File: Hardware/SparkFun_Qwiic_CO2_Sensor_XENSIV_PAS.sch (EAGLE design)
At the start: 39 parts, among them J1 QWIIC_RA, J2 QWIIC_RA, U1 PASCO2V01BUMA1, U2 LMR62421

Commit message: Update pre design review
Add keepouts for exposed pads.
Move vias to avoid keepouts.
Add 10k PUR to PSEL 3.3V selector.
Add voltage/current details to CO2 sensor on schematic.
Modified bottom PTHs to match standard order.
Move vias for ground pour.
Remove ground stub and unnecessary tRestrict.
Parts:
- added R7: 10k, SparkFun-Resistors:10KOHM-0603-1/10W-1%
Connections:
- new net N$8: PSEL.1, R7.1
- net 3.3V: now also J4.3, R7.2; no longer J4.2, PSEL.1
- net GND: now also J4.2; no longer J4.5
- net SCL: now also J4.5; no longer J4.4
- net SDA/TX: now also J4.4; no longer J4.3
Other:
- note added: "Power requirements: 3.3V - 10mA peak, 6.1mA average 12V - 130mA peak, 0.8mA average"
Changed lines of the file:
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@@
 <part name="GND14" library="SparkFun-PowerSymbols" deviceset="GND" device=""/>
 <part name="GND15" library="SparkFun-PowerSymbols" deviceset="GND" device=""/>
-<part name="GND16" library="SparkFun-PowerSymbols" deviceset="GND" device=""/>
-<part name="SUPPLY10" library="SparkFun-PowerSymbols" deviceset="3.3V" device=""/>
 <part name="SUPPLY11" library="SparkFun-PowerSymbols" deviceset="3.3V" device=""/>
 <part name="SUPPLY12" library="SparkFun-PowerSymbols" deviceset="3.3V" device=""/>
@@
 <part name="GND17" library="SparkFun-PowerSymbols" deviceset="GND" device=""/>
 <part name="PWR" library="SparkFun-Jumpers" deviceset="JUMPER-SMT_2_NC_TRACE" device="_SILK" package3d_urn="urn:adsk.eagle:package:39281/1"/>
+<part name="R7" library="SparkFun-Resistors" deviceset="10KOHM" device="-0603-1/10W-1%" value="10k"/>
+<part name="GND16" library="SparkFun-PowerSymbols" deviceset="GND" device=""/>
+<part name="SUPPLY10" library="SparkFun-PowerSymbols" deviceset="3.3V" device=""/>
 </parts>
 <sheets>
@@
 Output: 12V @ 350mA</text>
 <text x="48.26" y="96.52" size="1.778" layer="97" font="vector">7-bit unshifted address: 0x28</text>
+<text x="53.34" y="81.28" size="1.778" layer="97" font="vector">Power requirements:
+3.3V - 10mA peak, 6.1mA average
+12V - 130mA peak, 0.8mA average</text>
 </plain>
 <instances>
@@
 <attribute name="NAME" x="38.1" y="116.84" size="1.778" layer="95" font="vector" rot="MR180" align="center-right"/>
 </instance>
-<instance part="SUPPLY8" gate="G$1" x="40.64" y="124.46" smashed="yes">
-<attribute name="VALUE" x="40.64" y="127.254" size="1.778" layer="96" font="vector" align="bottom-center"/>
+<instance part="SUPPLY8" gate="G$1" x="40.64" y="137.16" smashed="yes">
+<attribute name="VALUE" x="40.64" y="139.954" size="1.778" layer="96" font="vector" align="bottom-center"/>
 </instance>
 <instance part="GND11" gate="1" x="40.64" y="106.68" smashed="yes">
@@
 <attribute name="VALUE" x="226.06" y="78.486" size="1.778" layer="96" font="vector" align="top-center"/>
 </instance>
-<instance part="GND16" gate="1" x="200.66" y="91.44" smashed="yes">
-<attribute name="VALUE" x="200.66" y="91.186" size="1.778" layer="96" font="vector" align="top-center"/>
-</instance>
-<instance part="SUPPLY10" gate="G$1" x="200.66" y="109.22" smashed="yes">
-<attribute name="VALUE" x="200.66" y="112.014" size="1.778" layer="96" font="vector" align="bottom-center"/>
-</instance>
 <instance part="SUPPLY11" gate="G$1" x="226.06" y="121.92" smashed="yes">
 <attribute name="VALUE" x="226.06" y="124.714" size="1.778" layer="96" font="vector" align="bottom-center"/>
@@
 <instance part="PWR" gate="G$1" x="154.94" y="137.16" smashed="yes" rot="R90">
 <attribute name="NAME" x="160.02" y="136.652" size="1.778" layer="95" font="vector" rot="R180" align="center"/>
+</instance>
+<instance part="R7" gate="G$1" x="40.64" y="129.54" smashed="yes" rot="R90">
+<attribute name="NAME" x="39.116" y="129.54" size="1.778" layer="95" font="vector" rot="R90" align="bottom-center"/>
+<attribute name="VALUE" x="42.164" y="129.54" size="1.778" layer="96" font="vector" rot="R90" align="top-center"/>
+</instance>
+<instance part="GND16" gate="1" x="203.2" y="88.9" smashed="yes">
+<attribute name="VALUE" x="203.2" y="88.646" size="1.778" layer="96" font="vector" align="top-center"/>
+</instance>
+<instance part="SUPPLY10" gate="G$1" x="200.66" y="109.22" smashed="yes">
+<attribute name="VALUE" x="200.66" y="112.014" size="1.778" layer="96" font="vector" align="bottom-center"/>
 </instance>
 </instances>
@@
 </segment>
 <segment>
-<wire x1="200.66" y1="96.52" x2="200.66" y2="93.98" width="0.1524" layer="91"/>
-<pinref part="GND16" gate="1" pin="GND"/>
-<pinref part="J4" gate="J1" pin="5"/>
-<wire x1="198.12" y1="96.52" x2="200.66" y2="96.52" width="0.1524" layer="91"/>
-</segment>
-<segment>
 <wire x1="226.06" y1="142.24" x2="226.06" y2="137.16" width="0.1524" layer="91"/>
 <pinref part="GND12" gate="1" pin="GND"/>
@@
 <wire x1="154.94" y1="109.22" x2="154.94" y2="106.68" width="0.1524" layer="91"/>
 <pinref part="GND17" gate="1" pin="GND"/>
+</segment>
+<segment>
+<wire x1="203.2" y1="104.14" x2="203.2" y2="91.44" width="0.1524" layer="91"/>
+<pinref part="GND16" gate="1" pin="GND"/>
+<wire x1="198.12" y1="104.14" x2="203.2" y2="104.14" width="0.1524" layer="91"/>
+<pinref part="J4" gate="J1" pin="2"/>
 </segment>
 </net>
@@
 </segment>
 <segment>
-<pinref part="SUPPLY8" gate="G$1" pin="3.3V"/>
-<wire x1="40.64" y1="124.46" x2="40.64" y2="121.92" width="0.1524" layer="91"/>
-<pinref part="PSEL" gate="G$1" pin="1"/>
-</segment>
-<segment>
-<pinref part="SUPPLY10" gate="G$1" pin="3.3V"/>
-<wire x1="200.66" y1="109.22" x2="200.66" y2="104.14" width="0.1524" layer="91"/>
-<pinref part="J4" gate="J1" pin="2"/>
-<wire x1="198.12" y1="104.14" x2="200.66" y2="104.14" width="0.1524" layer="91"/>
-</segment>
-<segment>
 <pinref part="SUPPLY11" gate="G$1" pin="3.3V"/>
 <wire x1="226.06" y1="121.92" x2="226.06" y2="114.3" width="0.1524" layer="91"/>
@@
 <pinref part="SUPPLY13" gate="G$1" pin="3.3V"/>
 <wire x1="154.94" y1="142.24" x2="154.94" y2="144.78" width="0.1524" layer="91"/>
+</segment>
+<segment>
+<pinref part="SUPPLY8" gate="G$1" pin="3.3V"/>
+<pinref part="R7" gate="G$1" pin="2"/>
+<wire x1="40.64" y1="137.16" x2="40.64" y2="134.62" width="0.1524" layer="91"/>
+</segment>
+<segment>
+<pinref part="SUPPLY10" gate="G$1" pin="3.3V"/>
+<wire x1="200.66" y1="109.22" x2="200.66" y2="101.6" width="0.1524" layer="91"/>
+<wire x1="198.12" y1="101.6" x2="200.66" y2="101.6" width="0.1524" layer="91"/>
+<pinref part="J4" gate="J1" pin="3"/>
 </segment>
 </net>
@@
 <segment>
 <wire x1="198.12" y1="106.68" x2="203.2" y2="106.68" width="0.1524" layer="91"/>
+<label x="203.2" y="106.68" size="1.27" layer="95" font="vector" xref="yes"/>
 <pinref part="J4" gate="J1" pin="1"/>
-<label x="203.2" y="106.68" size="1.27" layer="95" font="vector" xref="yes"/>
 </segment>
 </net>
@@
 </segment>
 <segment>
-<wire x1="218.44" y1="91.44" x2="218.44" y2="99.06" width="0.1524" layer="91"/>
 <pinref part="J1" gate="J1" pin="4"/>
-<wire x1="218.44" y1="99.06" x2="218.44" y2="119.38" width="0.1524" layer="91"/>
+<wire x1="218.44" y1="91.44" x2="218.44" y2="96.52" width="0.1524" layer="91"/>
+<wire x1="218.44" y1="96.52" x2="218.44" y2="119.38" width="0.1524" layer="91"/>
 <wire x1="218.44" y1="119.38" x2="228.6" y2="119.38" width="0.1524" layer="91"/>
 <pinref part="J2" gate="J1" pin="4"/>
@@
 <junction x="218.44" y="119.38"/>
 <label x="215.9" y="119.38" size="1.27" layer="95" font="vector" rot="R180" xref="yes"/>
-<pinref part="J4" gate="J1" pin="4"/>
-<wire x1="198.12" y1="99.06" x2="218.44" y2="99.06" width="0.1524" layer="91"/>
-<junction x="218.44" y="99.06"/>
+<wire x1="198.12" y1="96.52" x2="218.44" y2="96.52" width="0.1524" layer="91"/>
+<pinref part="J4" gate="J1" pin="5"/>
+<junction x="218.44" y="96.52"/>
 </segment>
 </net>
@@
 <wire x1="228.6" y1="116.84" x2="220.98" y2="116.84" width="0.1524" layer="91"/>
 <pinref part="J2" gate="J1" pin="3"/>
-<wire x1="220.98" y1="116.84" x2="220.98" y2="101.6" width="0.1524" layer="91"/>
-<wire x1="220.98" y1="101.6" x2="220.98" y2="88.9" width="0.1524" layer="91"/>
+<wire x1="220.98" y1="116.84" x2="220.98" y2="99.06" width="0.1524" layer="91"/>
+<wire x1="220.98" y1="99.06" x2="220.98" y2="88.9" width="0.1524" layer="91"/>
 <wire x1="220.98" y1="88.9" x2="228.6" y2="88.9" width="0.1524" layer="91"/>
-<pinref part="J4" gate="J1" pin="3"/>
-<wire x1="198.12" y1="101.6" x2="220.98" y2="101.6" width="0.1524" layer="91"/>
-<junction x="220.98" y="101.6"/>
 <wire x1="220.98" y1="116.84" x2="215.9" y2="116.84" width="0.1524" layer="91"/>
 <junction x="220.98" y="116.84"/>
 <label x="215.9" y="116.84" size="1.27" layer="95" font="vector" rot="R180" xref="yes"/>
+<wire x1="198.12" y1="99.06" x2="220.98" y2="99.06" width="0.1524" layer="91"/>
+<pinref part="J4" gate="J1" pin="4"/>
+<junction x="220.98" y="99.06"/>
 </segment>
 <segment>
@@
 </segment>
 </net>
+<net name="N$8" class="0">
+<segment>
+<pinref part="R7" gate="G$1" pin="1"/>
+<pinref part="PSEL" gate="G$1" pin="1"/>
+<wire x1="40.64" y1="124.46" x2="40.64" y2="121.92" width="0.1524" layer="91"/>
+</segment>
+</net>

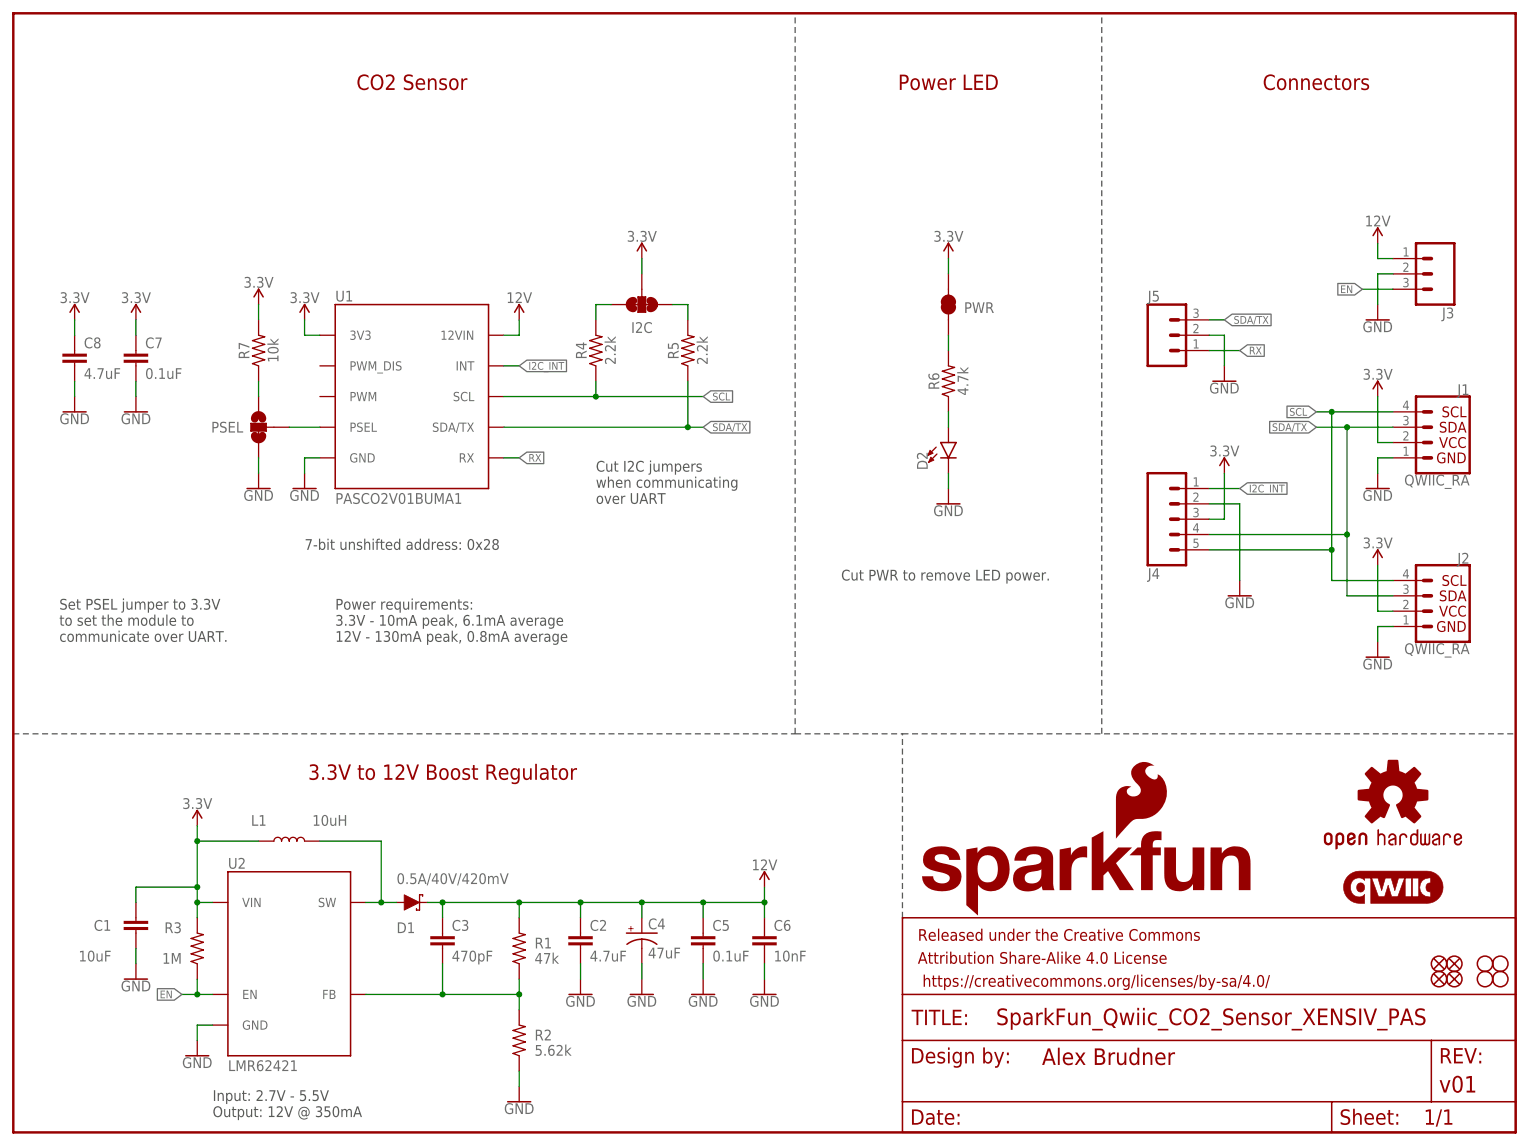
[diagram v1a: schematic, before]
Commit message: Post design review changes and gerbers.
Add tDocu for the can and put squares for PnP.
Move EN to bottom row.
Rearrange I2C PTHs on bottom row to align with prior art.
Add PWM/PWM_DIS breakout.
Change silk on 12V to 12VIN.
Shift vertical PTHs down 0.05 to line up with perfboard holes.
Create gerbers.
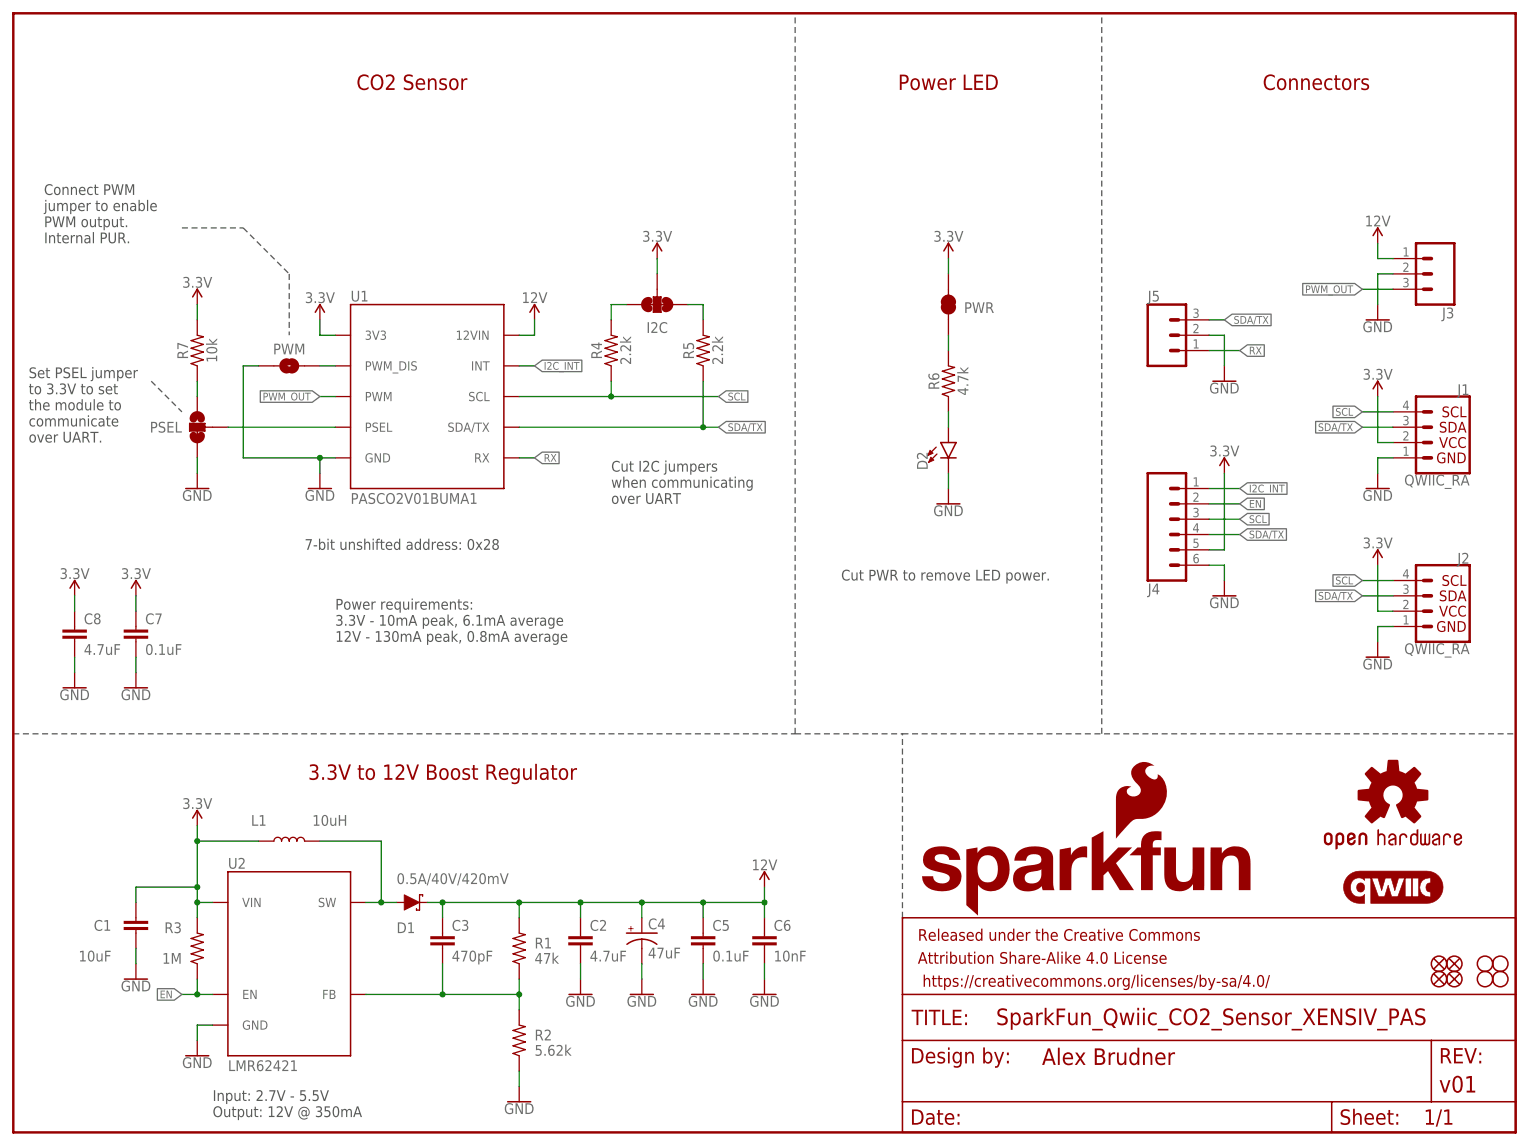
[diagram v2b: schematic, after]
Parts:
- added PWM: JUMPER-SMT_2_NO_SILK, SparkFun-Jumpers:JUMPER-SMT_2_NO_SILK
- J4: device SparkFun-Connectors:CONN_05NO_SILK -> SparkFun-Connectors:CONN_06NO_SILK_NO_POP
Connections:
- new net N$9: PWM.2, U1.PWM_DIS
- new net PWM_OUT: J3.3, U1.PWM
- net 3.3V: now also J4.5; no longer J4.3
- net EN: now also J4.2; no longer J3.3
- net GND: now also J4.6, PWM.1; no longer J4.2
- net SCL: now also J4.3; no longer J4.5
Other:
- note added: "Connect PWM jumper to enable PWM output. Internal PUR."
- moved on the sheet: C7, C8, I2C, PSEL, R4, R5, R7, U1
